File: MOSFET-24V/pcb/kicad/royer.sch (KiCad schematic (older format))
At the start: 24 parts, among them J1 9-24V, J2 COIL, Q1 IRFB4410, Q2 IRFD110, Q3 IRFD110, Q4 IRFB4410

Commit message: net labels
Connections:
- net D1: now reaches C1.1, C2.1, D1.2 (A), Q2.2 (D), R1.1
- net C1: now reaches C1.2, C6.2, D1.1 (K), J2.3, Q1.2 (D)
- net 9V: now reaches C5.1, D5.1 (K), Q2.1 (G), Q3.1 (G), R3.1, R4.1, R7.2
- net X2: now reaches D3.1 (K), Q2.3 (S), R3.2, R6.1
- net X1: now reaches D2.1 (K), Q3.3 (S), R2.1, R4.2
- net G1: now reaches Q1.1 (G), R2.2
- net D2: now reaches C3.1, C4.1, D4.2 (A), Q3.2 (D), R5.1
- net C2: now reaches C4.2, C6.1, D4.1 (K), J2.1, Q4.2 (D)
- net G2: now reaches Q4.1 (G), R6.2
- net 24V: now reaches J1.2, J2.2, R7.1
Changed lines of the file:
@@
 LIBS:contrib
 LIBS:valves
-LIBS:fluxgate
 LIBS:lamp
 LIBS:diode
@@
 	1    0    0    -1
 $EndComp
+Text Label 2350 5050 0    60   ~ 0
+C1
+Text Label 4450 5050 0    60   ~ 0
+C2
+Text Label 2700 5300 0    60   ~ 0
+G1
+Text Label 4000 5300 0    60   ~ 0
+G2
+Text Label 2850 4750 0    60   ~ 0
+D1
+Text Label 3850 4750 0    60   ~ 0
+D2
+Text Label 4050 4100 0    60   ~ 0
+9V
+Text Label 3200 5300 0    60   ~ 0
+X1
+Text Label 3600 5300 0    60   ~ 0
+X2
+Text Label 4750 3700 0    60   ~ 0
+24V
 $EndSCHEMATC

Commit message: rearranging SMD components
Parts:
- C5: footprint Capacitors_ThroughHole:C_Rect_L27_W9_H17_P23 -> Capacitors_SMD:c_elec_4x5.8
- C6: footprint Capacitors_ThroughHole:C_Rect_L27_W9_H17_P23 -> Capacitors_SMD:C_1206_HandSoldering
- D1, D4: footprint Diodes_SMD:MELF_Handsoldering -> Diodes_SMD:MiniMELF_Handsoldering
- Q1, Q4: footprint Housings_DIP:DIP-4_W7.62mm_LongPads -> TO_SOT_Packages_THT:TO-220_Neutral123_Vertical_LargePads
- Q2, Q3: footprint TO_SOT_Packages_THT:TO-220_Neutral123_Vertical_LargePads -> Housings_DIP:DIP-4_W7.62mm_LongPads
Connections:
- net C1: now also J2.1; no longer J2.3
- net C2: now also J2.3; no longer J2.1
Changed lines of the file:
@@
 F 0 "C5" H 4825 5000 50  0000 L CNN
 F 1 "1uF" H 4850 4800 50  0000 L CNN
-F 2 "Capacitors_ThroughHole:C_Rect_L27_W9_H17_P23" H 4838 4750 50  0001 C CNN
+F 2 "Capacitors_SMD:c_elec_4x5.8" H 4838 4750 50  0001 C CNN
 F 3 "" H 4800 4900 50  0000 C CNN
 	1    4800 4900
@@
 F 0 "C6" V 3350 3700 50  0000 L CNN
 F 1 "2uF" V 3350 4000 50  0000 L CNN
-F 2 "Capacitors_ThroughHole:C_Rect_L27_W9_H17_P23" H 3438 3750 50  0001 C CNN
+F 2 "Capacitors_SMD:C_1206_HandSoldering" H 3438 3750 50  0001 C CNN
 F 3 "" H 3400 3900 50  0000 C CNN
 	1    3400 3900
@@
 F 0 "Q1" H 2400 5400 50  0000 R CNN
 F 1 "IRFB4410" V 2700 5500 50  0000 R CNN
-F 2 "Housings_DIP:DIP-4_W7.62mm_LongPads" H 2650 5400 50  0001 C CNN
+F 2 "TO_SOT_Packages_THT:TO-220_Neutral123_Vertical_LargePads" H 2650 5400 50  0001 C CNN
 F 3 "" H 2450 5300 50  0000 C CNN
 	1    2450 5300
@@
 F 0 "Q3" V 3750 4600 50  0000 R CNN
 F 1 "IRFD110" V 4050 4550 50  0000 R CNN
-F 2 "TO_SOT_Packages_THT:TO-220_Neutral123_Vertical_LargePads" H 4000 4500 50  0001 C CNN
+F 2 "Housings_DIP:DIP-4_W7.62mm_LongPads" H 4000 4500 50  0001 C CNN
 F 3 "" H 3800 4400 50  0000 C CNN
 	1    3800 4400
@@
 F 0 "Q2" V 2950 4600 50  0000 R CNN
 F 1 "IRFD110" V 3250 4550 50  0000 R CNN
-F 2 "TO_SOT_Packages_THT:TO-220_Neutral123_Vertical_LargePads" H 3200 4500 50  0001 C CNN
+F 2 "Housings_DIP:DIP-4_W7.62mm_LongPads" H 3200 4500 50  0001 C CNN
 F 3 "" H 3000 4400 50  0000 C CNN
 	1    3000 4400
@@
 F 0 "Q4" H 4300 5400 50  0000 R CNN
 F 1 "IRFB4410" V 4600 5500 50  0000 R CNN
-F 2 "Housings_DIP:DIP-4_W7.62mm_LongPads" H 4550 5400 50  0001 C CNN
+F 2 "TO_SOT_Packages_THT:TO-220_Neutral123_Vertical_LargePads" H 4550 5400 50  0001 C CNN
 F 3 "" H 4350 5300 50  0000 C CNN
 	1    4350 5300
@@
 F 0 "D1" H 2550 4600 50  0000 C CNN
 F 1 "1N4148" H 2550 4400 50  0000 C CNN
-F 2 "Diodes_SMD:MELF_Handsoldering" H 2550 4500 50  0001 C CNN
+F 2 "Diodes_SMD:MiniMELF_Handsoldering" H 2550 4500 50  0001 C CNN
 F 3 "" H 2550 4500 50  0000 C CNN
 	1    2550 4500
@@
 F 0 "D4" H 4250 4600 50  0000 C CNN
 F 1 "1N4148" H 4250 4400 50  0000 C CNN
-F 2 "Diodes_SMD:MELF_Handsoldering" H 4250 4500 50  0001 C CNN
+F 2 "Diodes_SMD:MiniMELF_Handsoldering" H 4250 4500 50  0001 C CNN
 F 3 "" H 4250 4500 50  0000 C CNN
 	1    4250 4500
@@
 F 3 "" H 3375 3250 50  0001 C CNN
 	1    3400 3150
-	0    1    1    0
-$EndComp
-Wire Wire Line
+	0    -1   1    0
+$EndComp
+Wire Wire Line

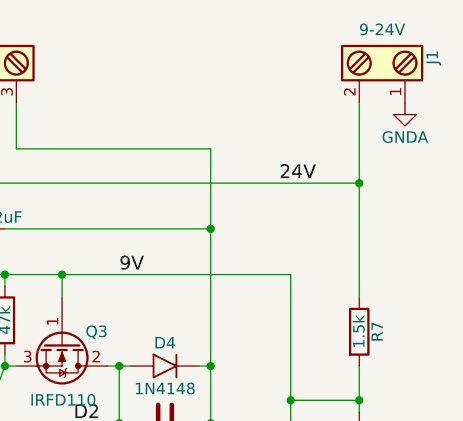
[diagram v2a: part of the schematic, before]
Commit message: fixing GND on the schematics
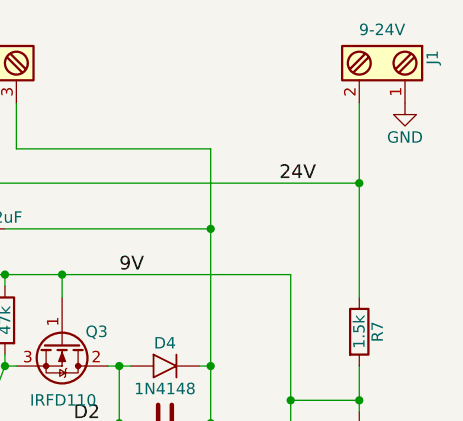
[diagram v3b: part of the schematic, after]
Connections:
- net GNDA is gone; now on net GND: J1.1
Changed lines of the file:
@@
 	0    1    1    0
-$EndComp
-$Comp
-L GNDA #PWR02
-U 1 1 58F35D3D
-P 5300 3350
-F 0 "#PWR02" H 5300 3100 50  0001 C CNN
-F 1 "GNDA" H 5300 3200 50  0000 C CNN
-F 2 "" H 5300 3350 50  0000 C CNN
-F 3 "" H 5300 3350 50  0000 C CNN
-	1    5300 3350
-	1    0    0    -1
 $EndComp
 Text Label 2350 5050 0    60   ~ 0
@@
 Text Label 4750 3700 0    60   ~ 0
 24V
+$Comp
+L GND #PWR?
+U 1 1 58F35A7F
+P 5300 3350
+F 0 "#PWR?" H 5300 3100 50  0001 C CNN
+F 1 "GND" H 5300 3200 50  0000 C CNN
+F 2 "" H 5300 3350 50  0000 C CNN
+F 3 "" H 5300 3350 50  0000 C CNN
+	1    5300 3350
+	1    0    0    -1
+$EndComp
 $EndSCHEMATC

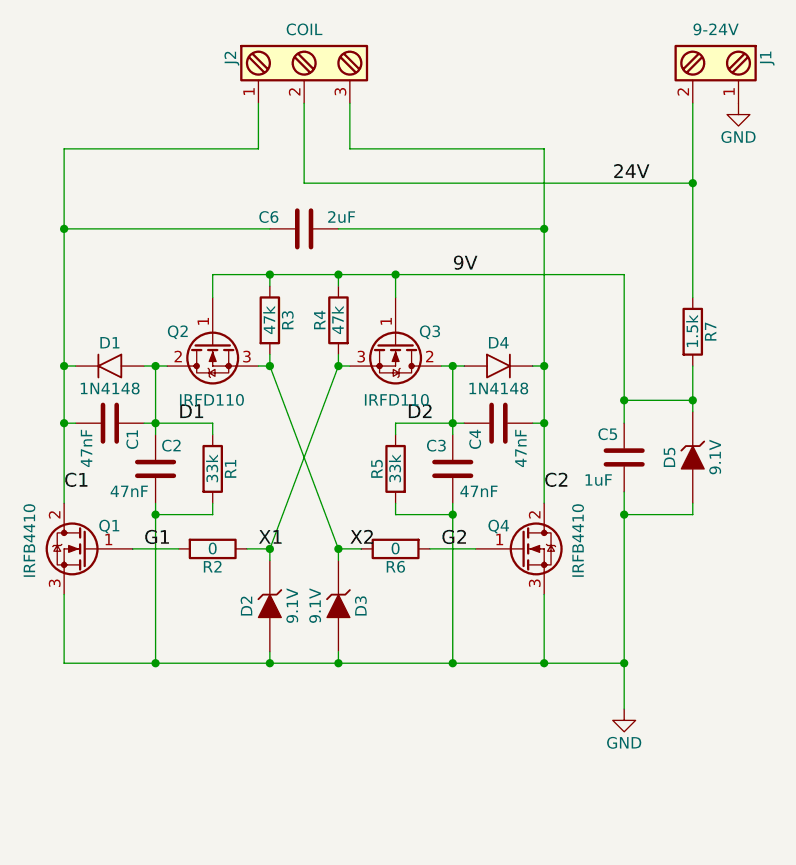
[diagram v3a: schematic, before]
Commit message: symmetry on the PCB
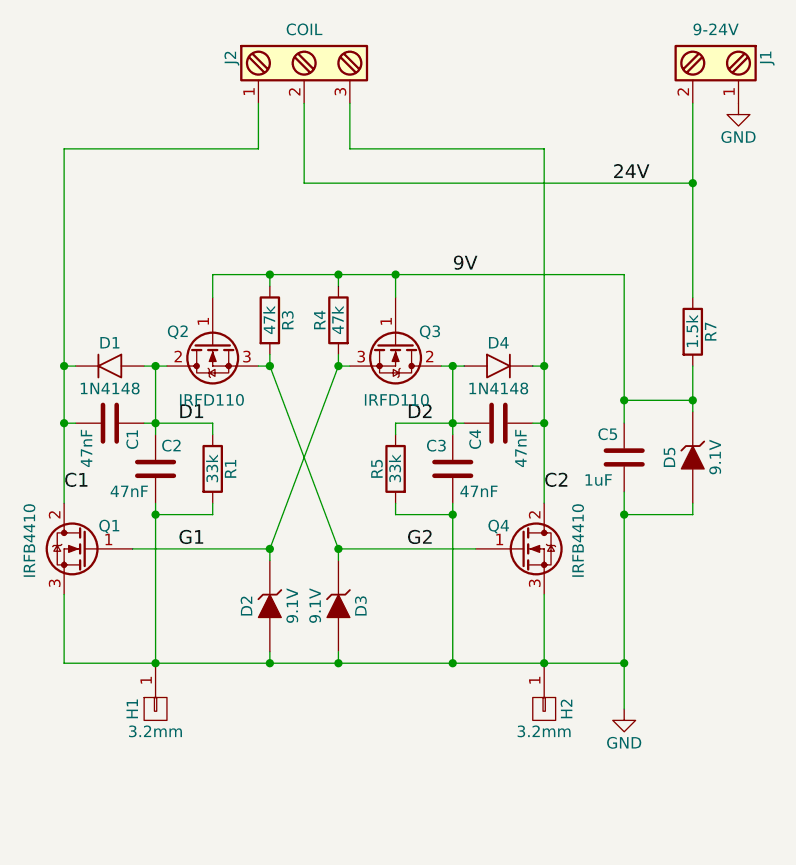
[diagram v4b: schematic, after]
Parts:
- removed C6: 2uF, Capacitors_SMD:C_1206_HandSoldering, symbol C
- removed R2, R6: 0, Resistors_SMD:R_1206_HandSoldering, symbol R
- added H1, H2: 3.2mm, Mounting_Holes:MountingHole_3.2mm_M3_ISO14580_Pad, symbol CONN_01X01
- Q1, Q4: footprint TO_SOT_Packages_THT:TO-220_Neutral123_Vertical_LargePads -> TO-220:TO-220_Neutral123_Horizontal_LargePads
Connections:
- net X1 is gone; now on net G1: D2.1 (K), Q3.3 (S), R4.2
- net X2 is gone; now on net G2: D3.1 (K), Q2.3 (S), R3.2
- net GND: now also H1.1 (P1), H2.1 (P1)
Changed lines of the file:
@@
-$EndComp
-$Comp
-L R R2
-U 1 1 58419092
-P 3000 5300
-F 0 "R2" V 3080 5300 50  0000 C CNN
-F 1 "0" V 3000 5300 50  0000 C CNN
-F 2 "Resistors_SMD:R_1206_HandSoldering" V 2930 5300 50  0001 C CNN
-F 3 "" H 3000 5300 50  0000 C CNN
-	1    3000 5300
-	0    1    1    0
 $EndComp
 $Comp
@@
 $EndComp
 $Comp
-L R R6
-U 1 1 58419AF3
-P 3800 5300
-F 0 "R6" V 3880 5300 50  0000 C CNN
-F 1 "0" V 3800 5300 50  0000 C CNN
-F 2 "Resistors_SMD:R_1206_HandSoldering" V 3730 5300 50  0001 C CNN
-F 3 "" H 3800 5300 50  0000 C CNN
-	1    3800 5300
-	0    -1   1    0
-$EndComp
-$Comp
 L C C5
 U 1 1 5841D866
@@
 	3250 4100 3250 4150
 Wire Wire Line
-	2650 5300 2850 5300
-Wire Wire Line
-	3150 5300 3250 5300
+	2650 5300 3250 5300
 Wire Wire Line
 	3250 5300 3550 4500
@@
 	3550 4100 3550 4150
 Wire Wire Line
-	4150 5300 3950 5300
-Wire Wire Line
-	3550 5300 3650 5300
+	3550 5300 4150 5300
 Wire Wire Line
 	3550 5300 3550 5350
@@
 Connection ~ 4800 5800
 $Comp
-L C C6
-U 1 1 58426E3E
-P 3400 3900
-F 0 "C6" V 3350 3700 50  0000 L CNN
-F 1 "2uF" V 3350 4000 50  0000 L CNN
-F 2 "Capacitors_SMD:C_1206_HandSoldering" H 3438 3750 50  0001 C CNN
-F 3 "" H 3400 3900 50  0000 C CNN
-	1    3400 3900
-	0    1    1    0
-$EndComp
-Wire Wire Line
-	3550 3900 4450 3900
-Wire Wire Line
-	2350 3900 3250 3900
-$Comp
 L ZENER D2
 U 1 1 58419259
@@
 F 0 "Q1" H 2400 5400 50  0000 R CNN
 F 1 "IRFB4410" V 2700 5500 50  0000 R CNN
-F 2 "TO_SOT_Packages_THT:TO-220_Neutral123_Vertical_LargePads" H 2650 5400 50  0001 C CNN
+F 2 "TO-220:TO-220_Neutral123_Horizontal_LargePads" H 2650 5400 50  0001 C CNN
 F 3 "" H 2450 5300 50  0000 C CNN
 	1    2450 5300
@@
 F 0 "Q4" H 4300 5400 50  0000 R CNN
 F 1 "IRFB4410" V 4600 5500 50  0000 R CNN
-F 2 "TO_SOT_Packages_THT:TO-220_Neutral123_Vertical_LargePads" H 4550 5400 50  0001 C CNN
+F 2 "TO-220:TO-220_Neutral123_Horizontal_LargePads" H 4550 5400 50  0001 C CNN
 F 3 "" H 4350 5300 50  0000 C CNN
 	1    4350 5300
@@
 Wire Wire Line
 	3200 3550 3200 3350
-Connection ~ 2350 3900
 Wire Wire Line
 	3600 3350 3600 3550
 Wire Wire Line
 	3600 3550 4450 3550
-Connection ~ 4450 3900
 Wire Wire Line
 	3400 3350 3400 3700
@@
 Text Label 4450 5050 0    60   ~ 0
 C2
-Text Label 2700 5300 0    60   ~ 0
+Text Label 2850 5300 0    60   ~ 0
 G1
-Text Label 4000 5300 0    60   ~ 0
+Text Label 3850 5300 0    60   ~ 0
 G2
 Text Label 2850 4750 0    60   ~ 0
@@
 Text Label 4050 4100 0    60   ~ 0
 9V
-Text Label 3200 5300 0    60   ~ 0
-X1
-Text Label 3600 5300 0    60   ~ 0
-X2
 Text Label 4750 3700 0    60   ~ 0
 24V
 $Comp
-L GND #PWR?
+L GND #PWR02
 U 1 1 58F35A7F
 P 5300 3350
-F 0 "#PWR?" H 5300 3100 50  0001 C CNN
+F 0 "#PWR02" H 5300 3100 50  0001 C CNN
 F 1 "GND" H 5300 3200 50  0000 C CNN
 F 2 "" H 5300 3350 50  0000 C CNN
@@
 	1    0    0    -1
 $EndComp
+$Comp
+L CONN_01X01 H2
+U 1 1 58F3D143
+P 4450 6000
+F 0 "H2" H 4450 6100 50  0000 C CNN
+F 1 "3.2mm" V 4550 6000 50  0000 C CNN
+F 2 "Mounting_Holes:MountingHole_3.2mm_M3_ISO14580_Pad" H 4450 6000 50  0001 C CNN
+F 3 "" H 4450 6000 50  0000 C CNN
+	1    4450 6000
+	0    1    1    0
+$EndComp
+$Comp
+L CONN_01X01 H1
+U 1 1 58F3D67A
+P 2750 6000
+F 0 "H1" H 2750 6100 50  0000 C CNN
+F 1 "3.2mm" V 2850 6000 50  0000 C CNN
+F 2 "Mounting_Holes:MountingHole_3.2mm_M3_ISO14580_Pad" H 2750 6000 50  0001 C CNN
+F 3 "" H 2750 6000 50  0000 C CNN
+	1    2750 6000
+	0    -1   1    0
+$EndComp
 $EndSCHEMATC

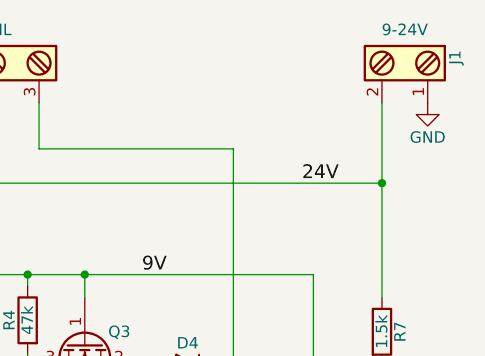
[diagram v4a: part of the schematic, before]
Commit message: rearranging components, routed
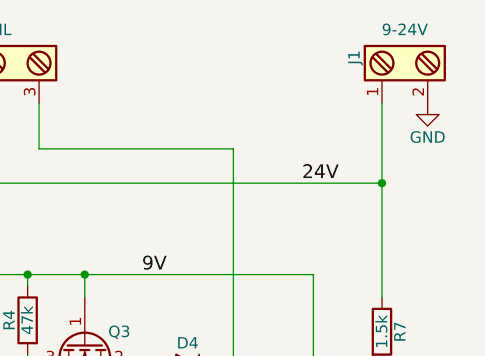
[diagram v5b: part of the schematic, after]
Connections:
- net 24V: now also J1.1; no longer J1.2
- net GND: now also J1.2; no longer J1.1
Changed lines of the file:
@@
 F 3 "" H 5175 3150 50  0001 C CNN
 	1    5200 3150
-	0    1    1    0
+	0    -1   1    0
 $EndComp
 Text Label 2350 5050 0    60   ~ 0

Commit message: optimizing component placement
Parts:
- added H3, H4: 3.2mm, Mounting_Holes:MountingHole_3.2mm_M3_ISO14580_Pad, symbol CONN_01X01
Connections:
- net GND: now also H3.1 (P1), H4.1 (P1)
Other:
- moved on the sheet: H1, H2
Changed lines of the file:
@@
 L CONN_01X01 H2
 U 1 1 58F3D143
-P 4450 6000
-F 0 "H2" H 4450 6100 50  0000 C CNN
-F 1 "3.2mm" V 4550 6000 50  0000 C CNN
-F 2 "Mounting_Holes:MountingHole_3.2mm_M3_ISO14580_Pad" H 4450 6000 50  0001 C CNN
-F 3 "" H 4450 6000 50  0000 C CNN
-	1    4450 6000
-	0    1    1    0
+P 3250 6200
+F 0 "H2" H 3250 6300 50  0000 C CNN
+F 1 "3.2mm" V 3350 6200 50  0000 C CNN
+F 2 "Mounting_Holes:MountingHole_3.2mm_M3_ISO14580_Pad" H 3250 6200 50  0001 C CNN
+F 3 "" H 3250 6200 50  0000 C CNN
+	1    3250 6200
+	0    -1   -1   0
 $EndComp
 $Comp
 L CONN_01X01 H1
 U 1 1 58F3D67A
-P 2750 6000
-F 0 "H1" H 2750 6100 50  0000 C CNN
-F 1 "3.2mm" V 2850 6000 50  0000 C CNN
-F 2 "Mounting_Holes:MountingHole_3.2mm_M3_ISO14580_Pad" H 2750 6000 50  0001 C CNN
-F 3 "" H 2750 6000 50  0000 C CNN
-	1    2750 6000
-	0    -1   1    0
+P 2900 6200
+F 0 "H1" H 2900 6300 50  0000 C CNN
+F 1 "3.2mm" V 3000 6200 50  0000 C CNN
+F 2 "Mounting_Holes:MountingHole_3.2mm_M3_ISO14580_Pad" H 2900 6200 50  0001 C CNN
+F 3 "" H 2900 6200 50  0000 C CNN
+	1    2900 6200
+	0    1    -1   0
+$EndComp
+$Comp
+L CONN_01X01 H4
+U 1 1 58F46EFD
+P 3900 6200
+F 0 "H4" H 3900 6300 50  0000 C CNN
+F 1 "3.2mm" V 4000 6200 50  0000 C CNN
+F 2 "Mounting_Holes:MountingHole_3.2mm_M3_ISO14580_Pad" H 3900 6200 50  0001 C CNN
+F 3 "" H 3900 6200 50  0000 C CNN
+	1    3900 6200
+	0    -1   -1   0
+$EndComp
+$Comp
+L CONN_01X01 H3
+U 1 1 58F46F03
+P 3550 6200
+F 0 "H3" H 3550 6300 50  0000 C CNN
+F 1 "3.2mm" V 3650 6200 50  0000 C CNN
+F 2 "Mounting_Holes:MountingHole_3.2mm_M3_ISO14580_Pad" H 3550 6200 50  0001 C CNN
+F 3 "" H 3550 6200 50  0000 C CNN
+	1    3550 6200
+	0    1    -1   0
+$EndComp
+$Comp
+L GND #PWR03
+U 1 1 58F46F6F
+P 2900 6400
+F 0 "#PWR03" H 2900 6150 50  0001 C CNN
+F 1 "GND" H 2900 6250 50  0000 C CNN
+F 2 "" H 2900 6400 50  0000 C CNN
+F 3 "" H 2900 6400 50  0000 C CNN
+	1    2900 6400
+	1    0    0    -1
+$EndComp
+$Comp
+L GND #PWR04
+U 1 1 58F47000
+P 3250 6400
+F 0 "#PWR04" H 3250 6150 50  0001 C CNN
+F 1 "GND" H 3250 6250 50  0000 C CNN
+F 2 "" H 3250 6400 50  0000 C CNN
+F 3 "" H 3250 6400 50  0000 C CNN
+	1    3250 6400
+	1    0    0    -1
+$EndComp
+$Comp
+L GND #PWR05
+U 1 1 58F47046
+P 3550 6400
+F 0 "#PWR05" H 3550 6150 50  0001 C CNN
+F 1 "GND" H 3550 6250 50  0000 C CNN
+F 2 "" H 3550 6400 50  0000 C CNN
+F 3 "" H 3550 6400 50  0000 C CNN
+	1    3550 6400
+	1    0    0    -1
+$EndComp
+$Comp
+L GND #PWR06
+U 1 1 58F470A5
+P 3900 6400
+F 0 "#PWR06" H 3900 6150 50  0001 C CNN
+F 1 "GND" H 3900 6250 50  0000 C CNN
+F 2 "" H 3900 6400 50  0000 C CNN
+F 3 "" H 3900 6400 50  0000 C CNN
+	1    3900 6400
+	1    0    0    -1
 $EndComp
 $EndSCHEMATC

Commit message: stack DIL-4 end-to-end to fit into a single DIL-8 socket
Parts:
- Q2, Q3: footprint Housings_DIP:DIP-4_W7.62mm_LongPads -> DIL-4:DIP-4_W7.62mm_LongPads
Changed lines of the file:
@@
 F 0 "Q3" V 3750 4600 50  0000 R CNN
 F 1 "IRFD110" V 4050 4550 50  0000 R CNN
-F 2 "Housings_DIP:DIP-4_W7.62mm_LongPads" H 4000 4500 50  0001 C CNN
+F 2 "DIL-4:DIP-4_W7.62mm_LongPads" H 4000 4500 50  0001 C CNN
 F 3 "" H 3800 4400 50  0000 C CNN
 	1    3800 4400
@@
 F 0 "Q2" V 2950 4600 50  0000 R CNN
 F 1 "IRFD110" V 3250 4550 50  0000 R CNN
-F 2 "Housings_DIP:DIP-4_W7.62mm_LongPads" H 3200 4500 50  0001 C CNN
+F 2 "DIL-4:DIP-4_W7.62mm_LongPads" H 3200 4500 50  0001 C CNN
 F 3 "" H 3000 4400 50  0000 C CNN
 	1    3000 4400

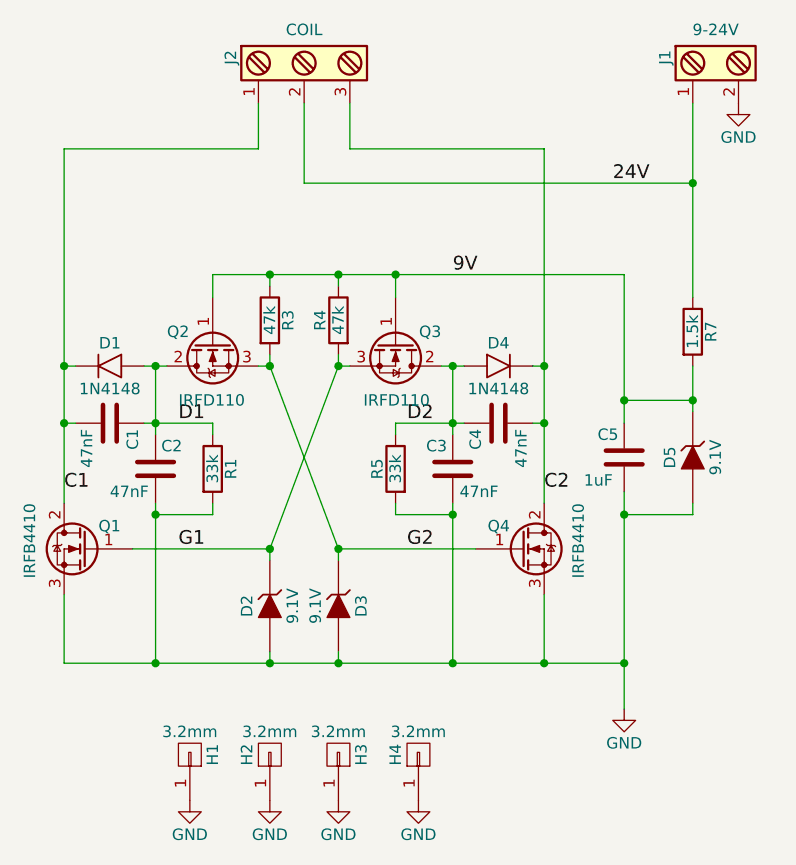
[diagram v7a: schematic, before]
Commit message: compacting PCB
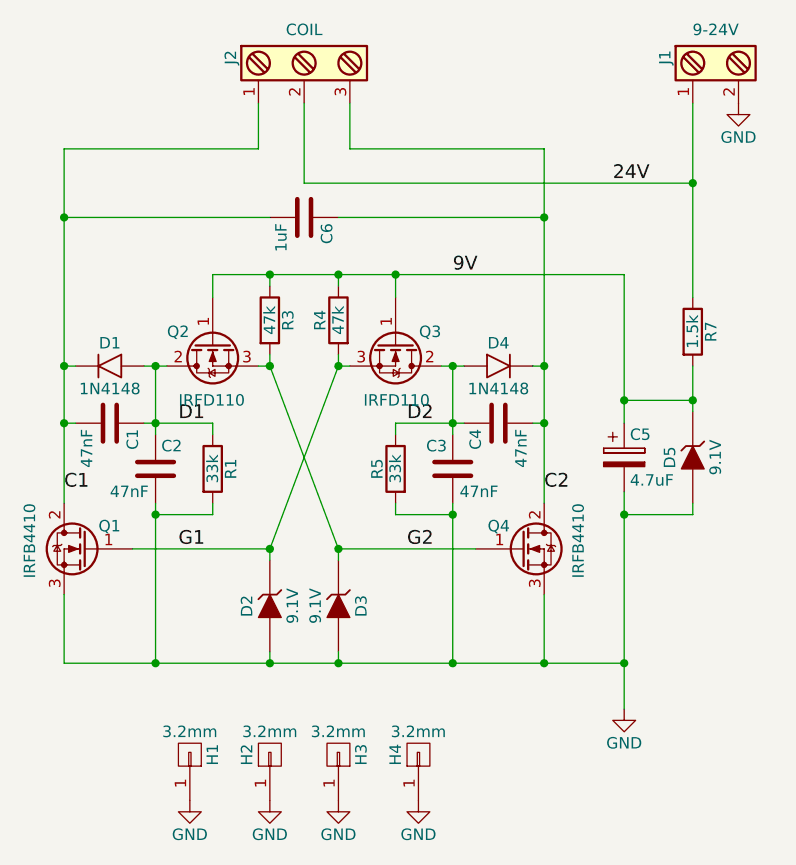
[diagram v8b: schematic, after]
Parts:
- removed C5: 1uF, Capacitors_SMD:c_elec_4x5.8, symbol C
- added C5: 4.7uF, Capacitors_Tantalum_SMD:Tantalum_Case-C_EIA-6032-28_Hand, symbol CP
- added C6: 1uF, Choke_Axial_ThroughHole:Choke_Horizontal_RM10mm, symbol C
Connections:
- net 9V: now also C5.1
- net C1: now also C6.2
- net C2: now also C6.1
- net GND: now also C5.2
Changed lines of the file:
@@
-	-1   0    0    -1
-$EndComp
-$Comp
-L C C5
-U 1 1 5841D866
-P 4800 4900
-F 0 "C5" H 4825 5000 50  0000 L CNN
-F 1 "1uF" H 4850 4800 50  0000 L CNN
-F 2 "Capacitors_SMD:c_elec_4x5.8" H 4838 4750 50  0001 C CNN
-F 3 "" H 4800 4900 50  0000 C CNN
-	1    4800 4900
 	-1   0    0    -1
 $EndComp
@@
 	1    0    0    -1
 $EndComp
+$Comp
+L C C6
+U 1 1 58F4917F
+P 3400 3850
+F 0 "C6" H 3425 3950 50  0000 L CNN
+F 1 "1uF" H 3425 3750 50  0000 L CNN
+F 2 "Choke_Axial_ThroughHole:Choke_Horizontal_RM10mm" H 3438 3700 50  0001 C CNN
+F 3 "" H 3400 3850 50  0000 C CNN
+	1    3400 3850
+	0    1    1    0
+$EndComp
+Wire Wire Line
+	3550 3850 4450 3850
+Connection ~ 4450 3850
+Wire Wire Line
+	3250 3850 2350 3850
+Connection ~ 2350 3850
+$Comp
+L CP C5
+U 1 1 58F49BFC
+P 4800 4900
+F 0 "C5" H 4825 5000 50  0000 L CNN
+F 1 "4.7uF" H 4825 4800 50  0000 L CNN
+F 2 "Capacitors_Tantalum_SMD:Tantalum_Case-C_EIA-6032-28_Hand" H 4838 4750 50  0001 C CNN
+F 3 "" H 4800 4900 50  0000 C CNN
+	1    4800 4900
+	1    0    0    -1
+$EndComp
